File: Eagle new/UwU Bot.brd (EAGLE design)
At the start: 75.9 x 81.3 mm, 8 parts, among them U1 173010535

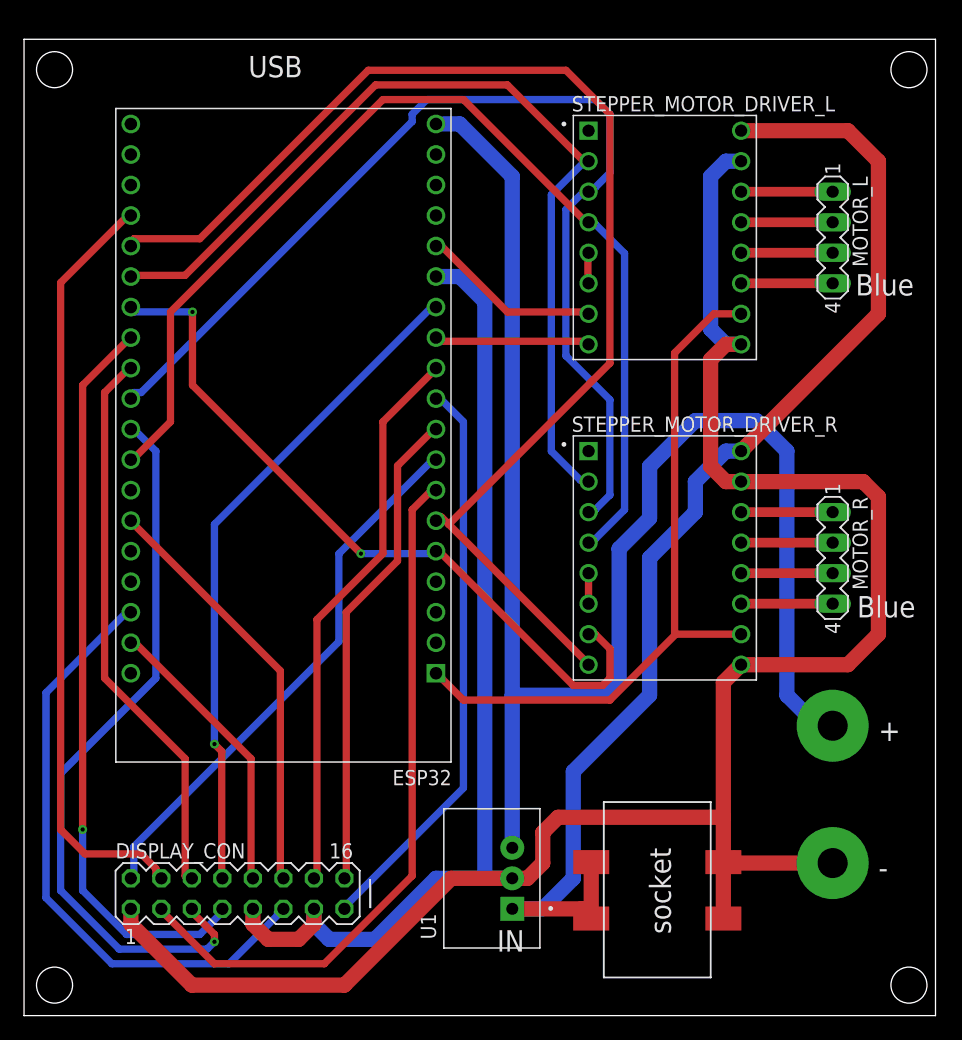
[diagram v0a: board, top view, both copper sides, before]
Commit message: cleanup and fixed hole size
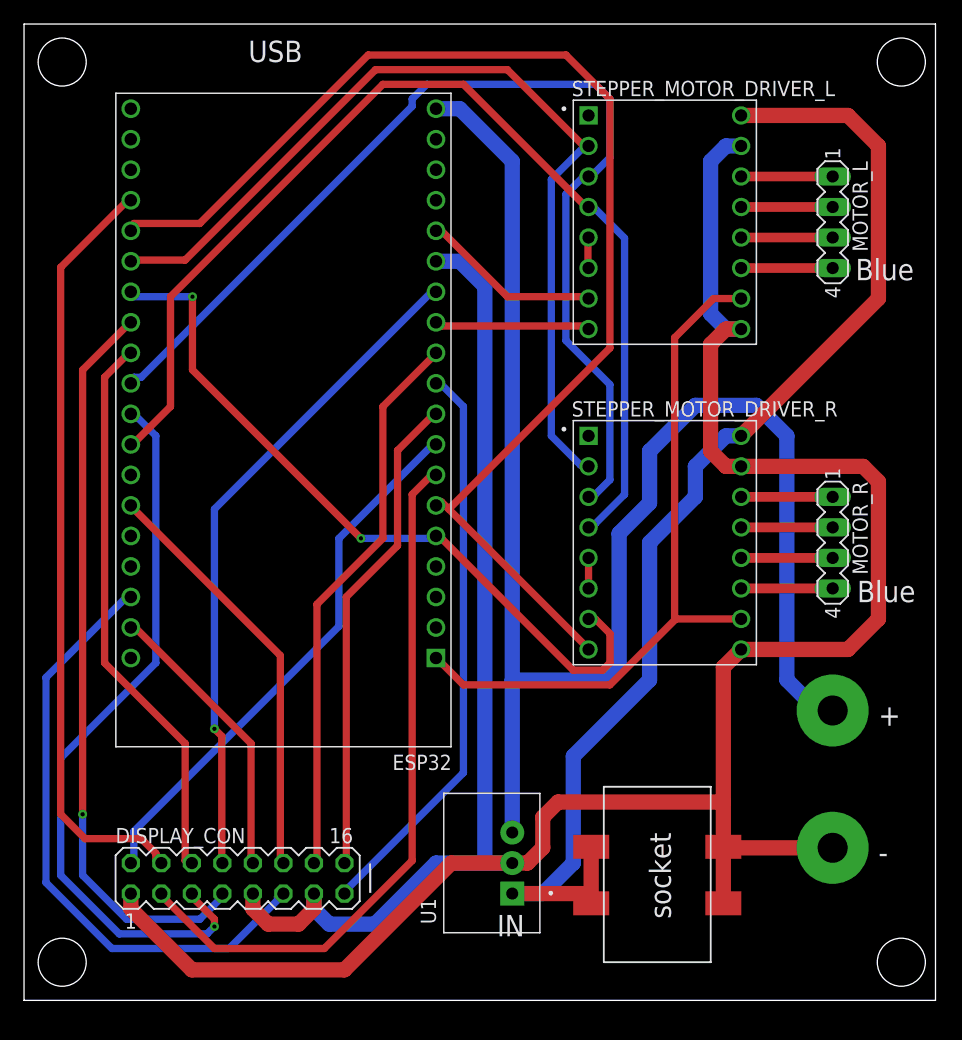
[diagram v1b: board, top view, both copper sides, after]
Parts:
- moved MOTOR_R 1.27 mm to (67.3, 38.1)
- moved STEPPER_MOTOR_DRIVER_R 1.27 mm to (53.3, 38.1)
- moved DISPLAY_CON 1.27 mm to (17.8, 10.2)
- moved U$1 1.27 mm to (48.3, 17.8)
- moved U1 1.27 mm to (40.6, 11.4)
- moved ESP32 1.27 mm to (21.6, 48.3)
- moved MOTOR_L 1.27 mm to (67.3, 64.8)
- moved STEPPER_MOTOR_DRIVER_L 1.27 mm to (53.3, 64.8)
